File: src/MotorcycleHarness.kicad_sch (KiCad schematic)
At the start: 16 parts, among them J36 Conn_01x02_Pin

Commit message: Update Schematics design
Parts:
- removed J?: MiniFit_2x04_F, Connector_Molex:Molex_Mini-Fit_Jr_5566-08A_2x04_P4.20mm_Vertical, symbol Connector_Generic:Conn_02x04_Counter_Clockwise
- added D? (x2): SK510, Diode_SMD:D_SMB_Handsoldering, symbol Diode:1N5400
- added J37: MiniFit_2x05_F, Connector_Molex:Molex_Mini-Fit_Jr_5566-10A_2x05_P4.20mm_Vertical, symbol Connector_Generic:Conn_02x05_Counter_Clockwise
- renumbered J36 to J45
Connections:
- net Accessory: now also J37.10 (Pin_10)
- net BSignal: now also J37.4 (Pin_4)
- net HBeam: now also J37.9 (Pin_9)
- net Key: now also J37.1 (Pin_1)
- net LBeam: now also J37.8 (Pin_8)
- net LBlinker: now also D?.1 (K), J37.3 (Pin_3)
- net PLight: now also J37.7 (Pin_7)
- net RBlinker: now also D?.1 (K), J37.2 (Pin_2)
- new net EBlinker: D?.2 (A), D?.2 (A), J37.5 (Pin_5)
- no-connect marks 0 -> 1
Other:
- moved on the sheet: J?

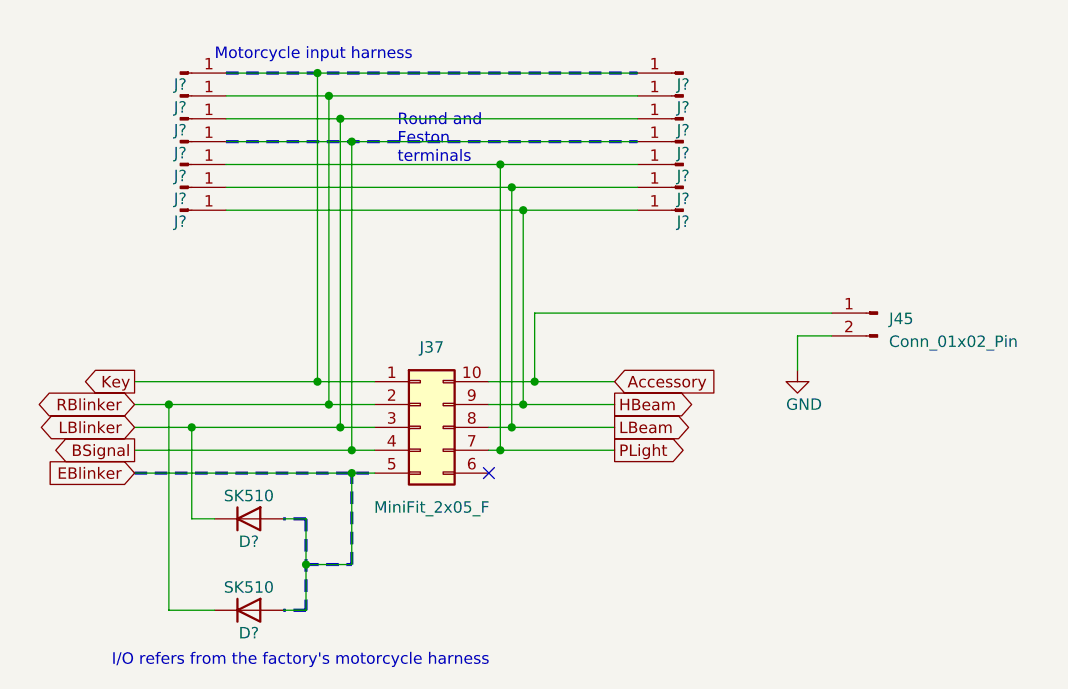
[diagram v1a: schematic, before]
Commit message: Add radio backup battery circuit; Update cable harness; rework main board circuit
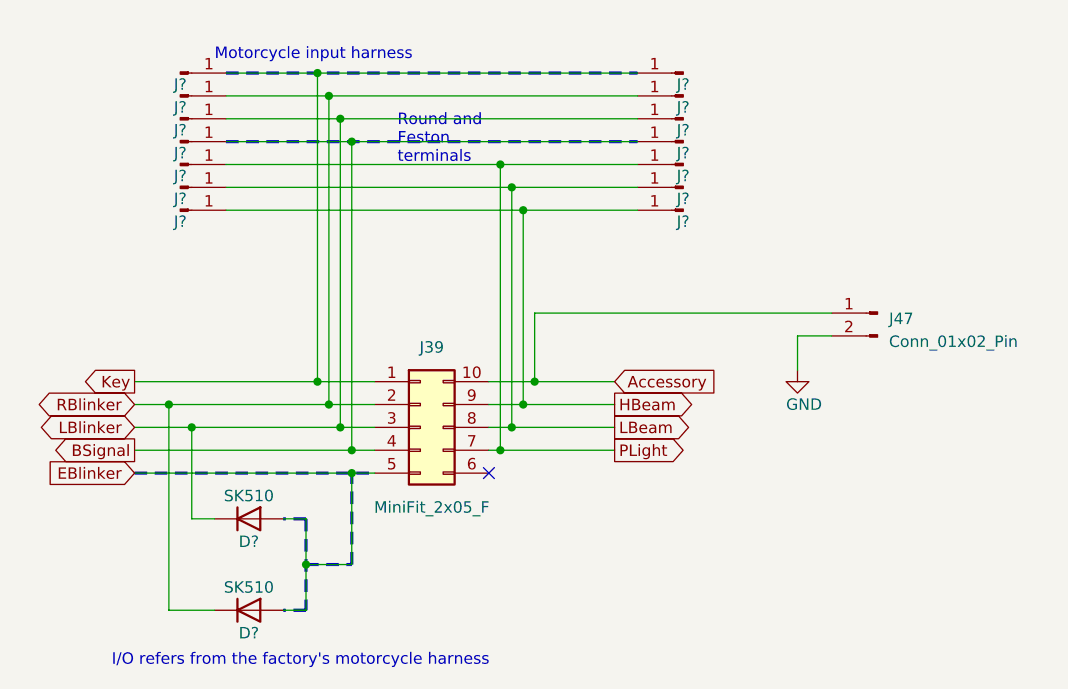
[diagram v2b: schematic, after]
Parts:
- renumbered J37 to J39, J45 to J47

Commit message: update Schematics
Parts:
- removed D? (x2): SK510, Diode_SMD:D_SMB_Handsoldering, symbol Diode:1N5400
- removed J39: MiniFit_2x05_F, Connector_Molex:Molex_Mini-Fit_Jr_5566-10A_2x05_P4.20mm_Vertical, symbol Connector_Generic:Conn_02x05_Counter_Clockwise
- removed J? (x2): Round, symbol Connector:Conn_01x01_Pin
- added J? (x14): Round, symbol Connector:Conn_01x01_Pin
- added J?: MiniFit_2x04_M, Connector_Molex:Molex_Mini-Fit_Jr_5566-08A_2x04_P4.20mm_Vertical, symbol Connector_Generic:Conn_02x04_Counter_Clockwise
- renumbered J47 to J41
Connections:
- net Accessory: now also J?.1 (Pin_1)
- net HBeam: now also J?.1 (Pin_1), J?.2 (Pin_2); no longer J?.1 (Pin_1), J?.1 (Pin_1)
- net Key: now also J?.1 (Pin_1), J?.8 (Pin_8); no longer J?.1 (Pin_1), J?.1 (Pin_1)
- net LBeam: now also J?.1 (Pin_1), J?.3 (Pin_3); no longer J?.1 (Pin_1), J?.1 (Pin_1)
- net LBlinker: now also J?.1 (Pin_1), J?.6 (Pin_6); no longer J?.1 (Pin_1), J?.1 (Pin_1)
- net PLight: now also J?.1 (Pin_1), J?.4 (Pin_4)
- net RBlinker: now also J?.1 (Pin_1), J?.7 (Pin_7); no longer J?.1 (Pin_1), J?.1 (Pin_1)
- net BSignal: no longer names the net of J?.1 (Pin_1), J?.1 (Pin_1)
- net BSignal: now also J?.1 (Pin_1)
- new net: J?.1 (Pin_1), J?.1 (Pin_1), J?.1 (Pin_1) (x5)
- new net SignalRelay: J?.1 (Pin_1), J?.5 (Pin_5)
- no-connect marks 1 -> 0
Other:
- note removed: "I/O refers from the factory's motorcycle harness"
- moved on the sheet: J?

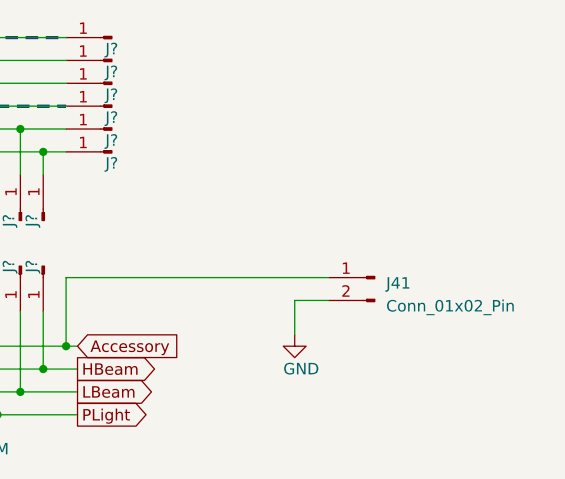
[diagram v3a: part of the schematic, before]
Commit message: Update Schmatics; Cleanup unecessary circuits; Simplify blinkers dimmers; Update PCB; Colorize motorcycle electric diagram.
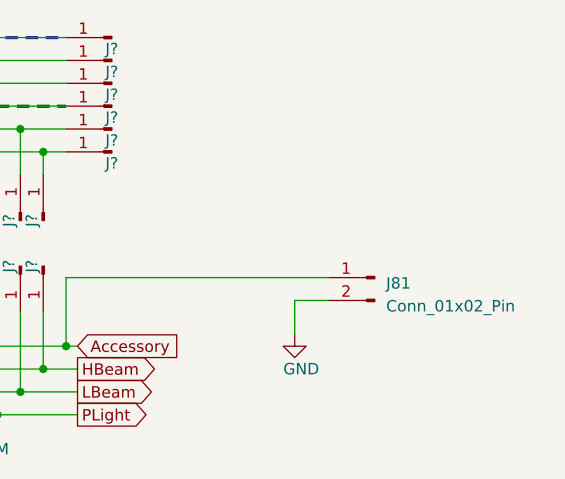
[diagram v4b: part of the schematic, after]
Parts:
- renumbered J41 to J81

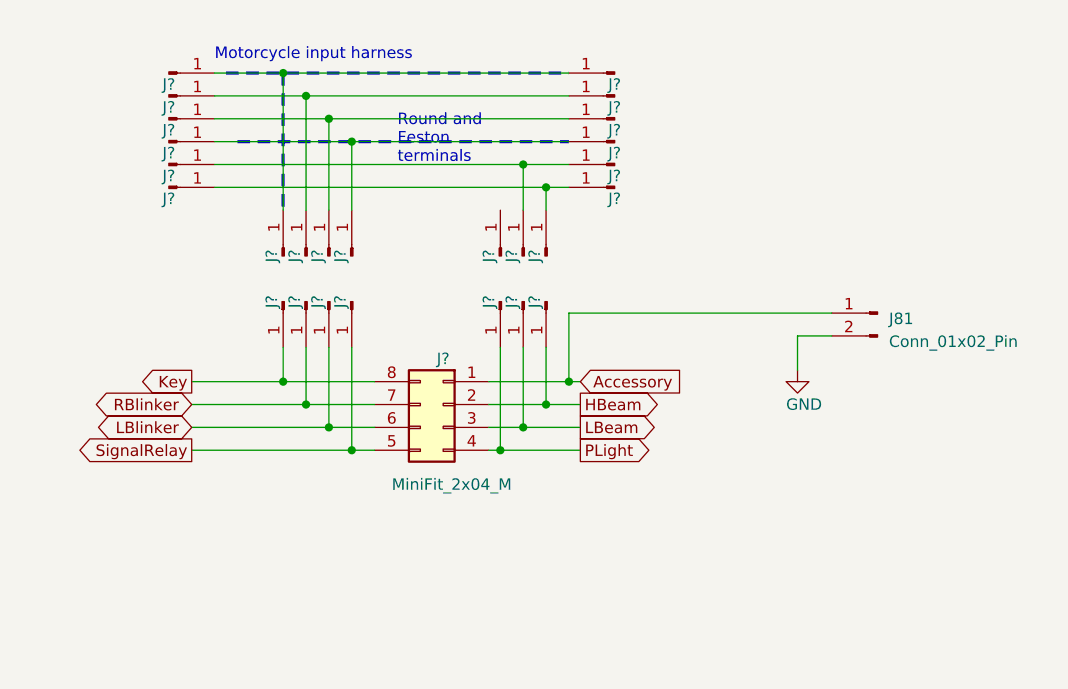
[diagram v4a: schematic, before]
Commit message: Update Schematics; Replace xor with quad nand; Update PCB
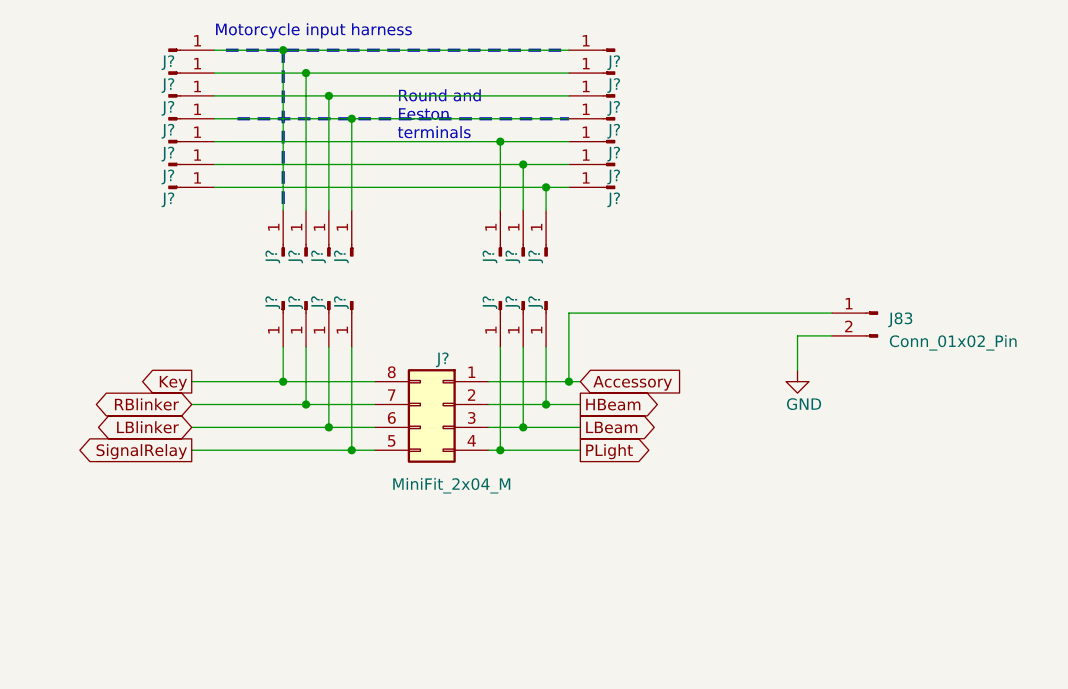
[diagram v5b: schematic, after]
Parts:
- added J? (x2): Round, symbol Connector:Conn_01x01_Pin
- renumbered J81 to J83
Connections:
- net at J?.1 (Pin_1): now also J?.1 (Pin_1), J?.1 (Pin_1)
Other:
- moved on the sheet: J?

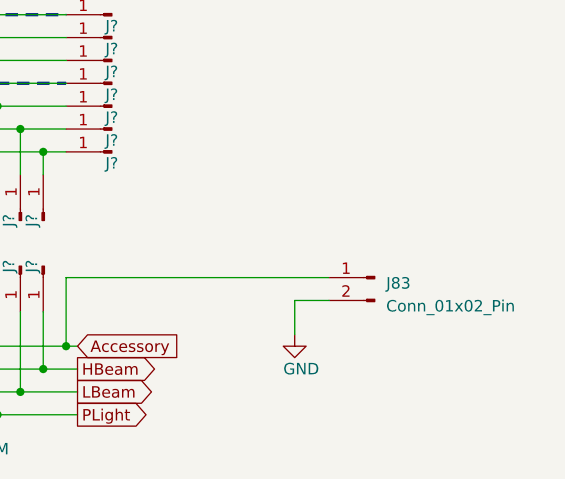
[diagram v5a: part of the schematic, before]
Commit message: simplify circuit diagram. Remove unecessary features; Split board into two components|
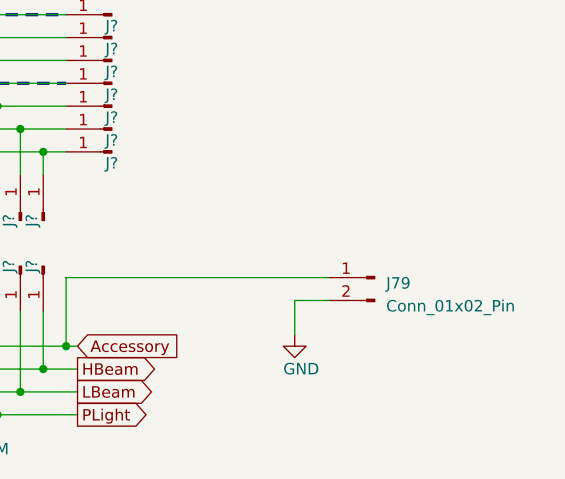
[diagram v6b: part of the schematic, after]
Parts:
- renumbered J83 to J79
